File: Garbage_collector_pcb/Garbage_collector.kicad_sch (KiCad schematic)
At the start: 0 parts

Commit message: seance 24 septembre
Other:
- sheet Alim ports: added GPOUT, I2C3_SCL, I2C3_SDA, INT, OTG, STAT, ~{PG}; removed none
- sheet Capteurs et périphériques ports: added I2C1_SCL, I2C1_SDA, Neo_Din, Neo_Dout; removed none
- sheet Moteurs ports: added AIN1, AIN2, BIN1, BIN2, M1_ENCA, M1_ENCB, M2_ENCA, M2_ENCB, Servo1, Servo2, Servo3, ~{FAULT}, ~{SLEEP}; removed none
- sheet STM32 ports: added I2C1_SCL, I2C1_SDA; removed none
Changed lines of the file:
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@@
+			)
+		)
+		(pin "I2C1_SCL" input
+			(at 127 64.77 0)
+			(effects
+				(font
+					(size 1.27 1.27)
+				)
+				(justify right)
+			)
+		)
+		(pin "I2C1_SDA" input
+			(at 127 68.58 0)
+			(effects
+				(font
+					(size 1.27 1.27)
+				)
+				(justify right)
 			)
 		)
@@
 			)
 		)
+		(pin "I2C1_SCL" input
+			(at 195.58 68.58 270)
+			(effects
+				(font
+					(size 1.27 1.27)
+				)
+				(justify left)
+			)
+		)
+		(pin "I2C1_SDA" input
+			(at 198.12 68.58 270)
+			(effects
+				(font
+					(size 1.27 1.27)
+				)
+				(justify left)
+			)
+		)
+		(pin "Neo_Din" input
+			(at 165.1 50.8 180)
+			(effects
+				(font
+					(size 1.27 1.27)
+				)
+				(justify left)
+			)
+		)
+		(pin "Neo_Dout" input
+			(at 165.1 54.61 180)
+			(effects
+				(font
+					(size 1.27 1.27)
+				)
+				(justify left)
+			)
+		)
 		(instances
 			(project "Garbage_collector"
@@
 			)
 		)
+		(pin "GPOUT" output
+			(at 165.1 93.98 180)
+			(effects
+				(font
+					(size 1.27 1.27)
+				)
+				(justify left)
+			)
+		)
+		(pin "I2C3_SCL" input
+			(at 165.1 99.06 180)
+			(effects
+				(font
+					(size 1.27 1.27)
+				)
+				(justify left)
+			)
+		)
+		(pin "I2C3_SDA" input
+			(at 165.1 102.87 180)
+			(effects
+				(font
+					(size 1.27 1.27)
+				)
+				(justify left)
+			)
+		)
+		(pin "INT" output
+			(at 165.1 106.68 180)
+			(effects
+				(font
+					(size 1.27 1.27)
+				)
+				(justify left)
+			)
+		)
+		(pin "OTG" input
+			(at 165.1 110.49 180)
+			(effects
+				(font
+					(size 1.27 1.27)
+				)
+				(justify left)
+			)
+		)
+		(pin "STAT" output
+			(at 165.1 115.57 180)
+			(effects
+				(font
+					(size 1.27 1.27)
+				)
+				(justify left)
+			)
+		)
+		(pin "~{PG}" output
+			(at 165.1 119.38 180)
+			(effects
+				(font
+					(size 1.27 1.27)
+				)
+				(justify left)
+			)
+		)
 		(instances
 			(project "Garbage_collector"
@@
 			)
 		)
+		(pin "AIN1" input
+			(at 128.27 124.46 0)
+			(effects
+				(font
+					(size 1.27 1.27)
+				)
+				(justify right)
+			)
+		)
+		(pin "AIN2" input
+			(at 128.27 127 0)
+			(effects
+				(font
+					(size 1.27 1.27)
+				)
+				(justify right)
+			)
+		)
+		(pin "BIN1" input
+			(at 128.27 129.54 0)
+			(effects
+				(font
+					(size 1.27 1.27)
+				)
+				(justify right)
+			)
+		)
+		(pin "BIN2" input
+			(at 128.27 132.08 0)
+			(effects
+				(font
+					(size 1.27 1.27)
+				)
+				(justify right)
+			)
+		)
+		(pin "M1_ENCA" input
+			(at 128.27 140.97 0)
+			(effects
+				(font
+					(size 1.27 1.27)
+				)
+				(justify right)
+			)
+		)
+		(pin "M1_ENCB" input
+			(at 128.27 143.51 0)
+			(effects
+				(font
+					(size 1.27 1.27)
+				)
+				(justify right)
+			)
+		)
+		(pin "M2_ENCA" input
+			(at 128.27 146.05 0)
+			(effects
+				(font
+					(size 1.27 1.27)
+				)
+				(justify right)
+			)
+		)
+		(pin "M2_ENCB" input
+			(at 128.27 148.59 0)
+			(effects
+				(font
+					(size 1.27 1.27)
+				)
+				(justify right)
+			)
+		)
+		(pin "Servo1" input
+			(at 128.27 113.03 0)
+			(effects
+				(font
+					(size 1.27 1.27)
+				)
+				(justify right)
+			)
+		)
+		(pin "Servo2" input
+			(at 128.27 115.57 0)
+			(effects
+				(font
+					(size 1.27 1.27)
+				)
+				(justify right)
+			)
+		)
+		(pin "Servo3" input
+			(at 128.27 118.11 0)
+			(effects
+				(font
+					(size 1.27 1.27)
+				)
+				(justify right)
+			)
+		)
+		(pin "~{FAULT}" input
+			(at 128.27 157.48 0)
+			(effects
+				(font
+					(size 1.27 1.27)
+				)
+				(justify right)
+			)
+		)
+		(pin "~{SLEEP}" input
+			(at 128.27 154.94 0)
+			(effects
+				(font
+					(size 1.27 1.27)
+				)
+				(justify right)
+			)
+		)

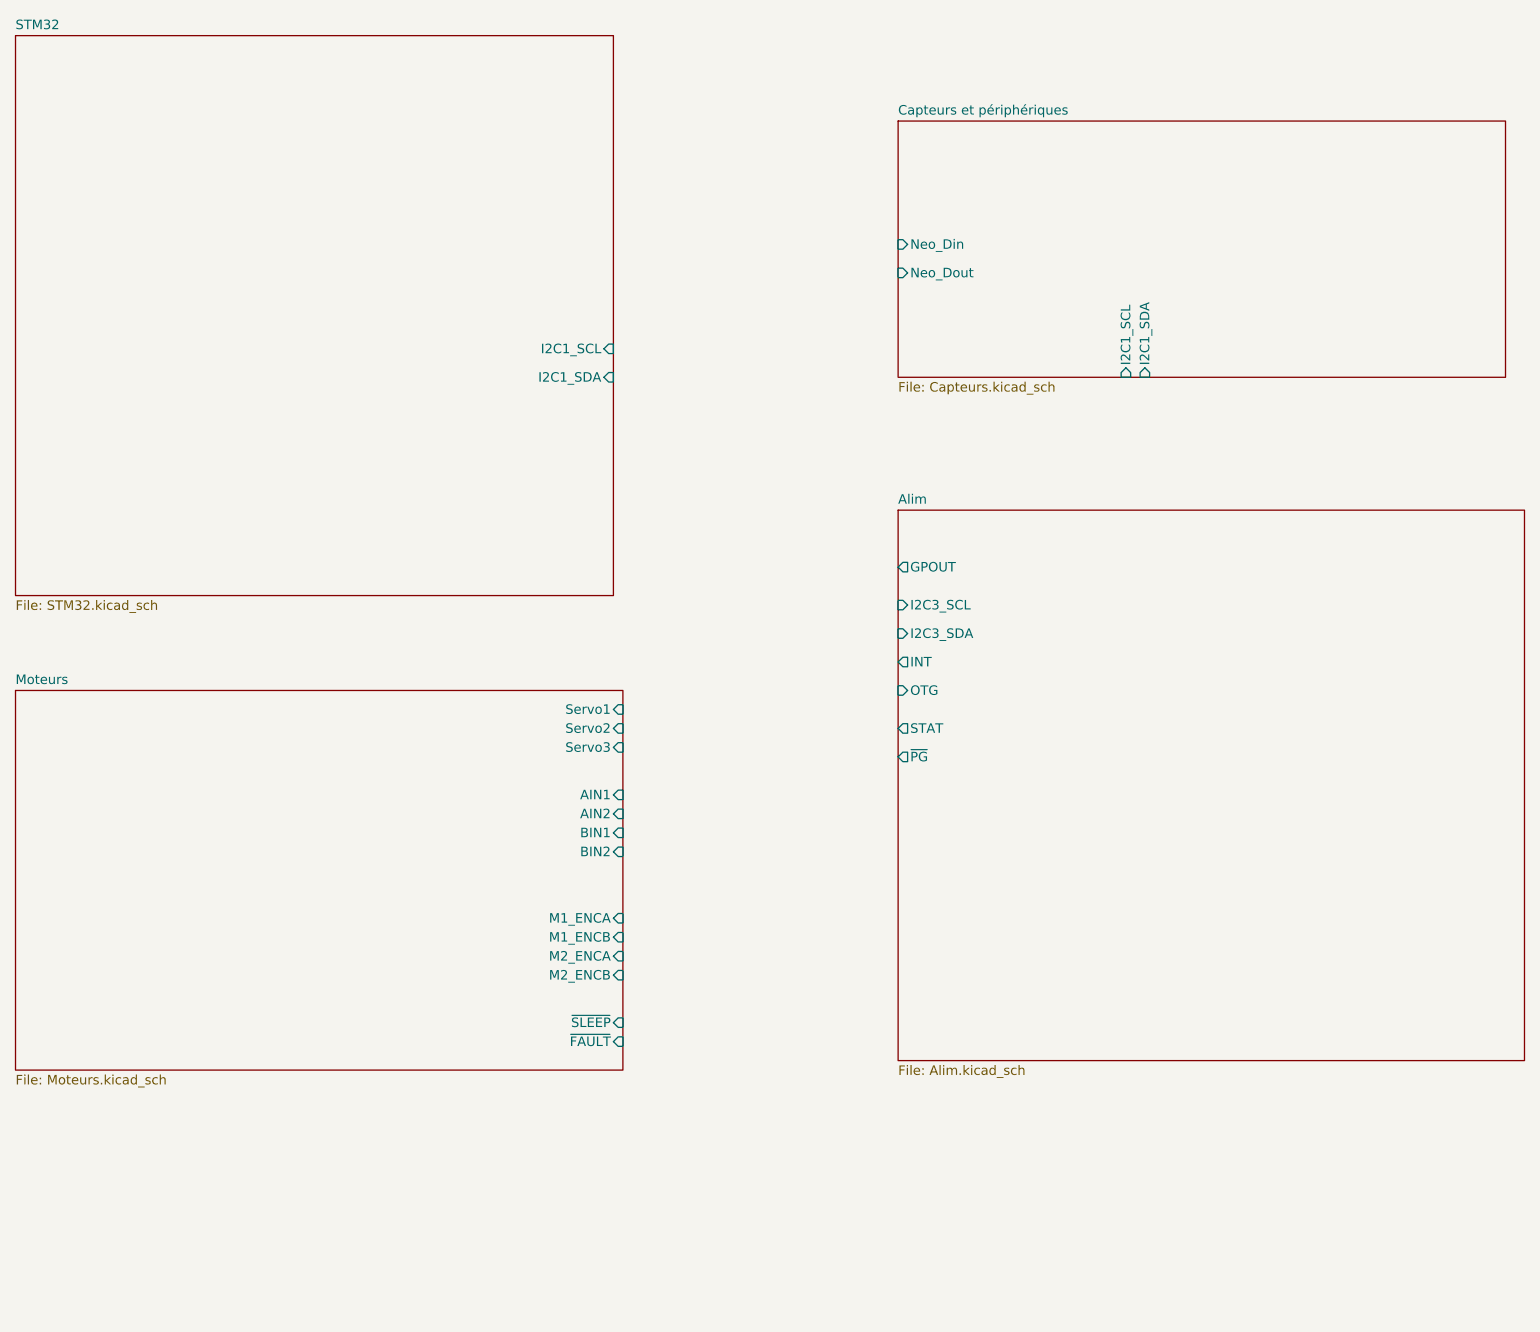
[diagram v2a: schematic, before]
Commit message: update MCU+Moteurs+Capteurs parts + assignement des labels + assignement des pins sur l'ioc (CubeMX)
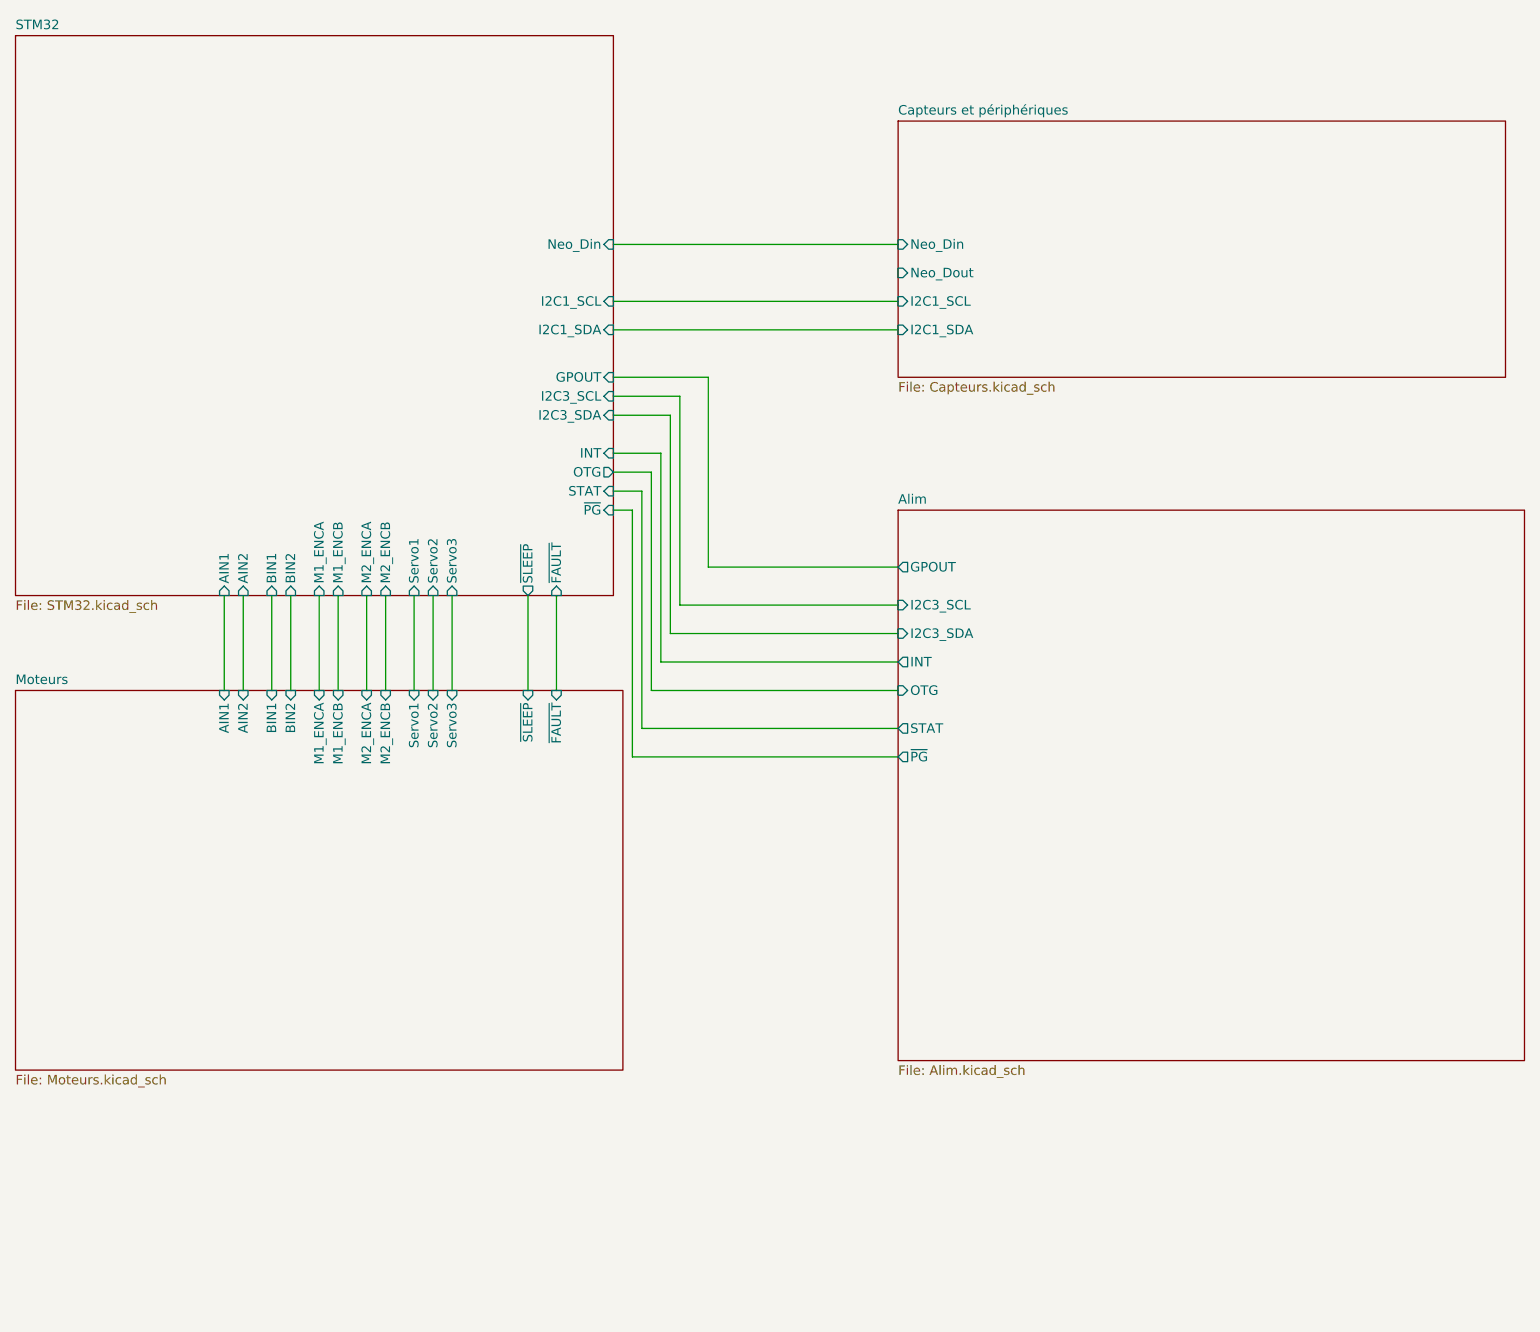
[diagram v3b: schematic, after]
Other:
- sheet STM32 ports: added AIN1, AIN2, BIN1, BIN2, GPOUT, I2C3_SCL, I2C3_SDA, INT, M1_ENCA, M1_ENCB, M2_ENCA, M2_ENCB, Neo_Din, OTG, STAT, Servo1, Servo2, Servo3, ~{FAULT}, ~{PG}, ~{SLEEP}; removed none

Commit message: ajout du ioc et schema validé
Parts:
- added H1, H2, H3, H4: MountingHole_Pad, MountingHole:MountingHole_3.2mm_M3_ISO14580_Pad, symbol Kicad:MountingHole_Pad
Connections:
- new net GND: H1.1, H2.1, H3.1, H4.1
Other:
- sheet Alim ports: added CHARGEUR_INT, CHARGEUR_PG, CHARGEUR_QON, FG_GPIO; removed GPOUT, INT, OTG, STAT, ~{PG}
- sheet Capteurs et périphériques ports: added COLOR_INT, Lidar_M_CTRL, Lidar_TX, TOF1_INT, TOF1_XST, TOF2_INT, TOF2_XST; removed Neo_Dout
- sheet Moteurs ports: added MOTOR_FAULT, MOTOR_SLEEP; removed Servo3, ~{FAULT}, ~{SLEEP}
- sheet STM32 ports: added CHARGEUR_INT, CHARGEUR_PG, COLOR_INT, FG_GPIO, Lidar_M_CTRL, Lidar_TX, MOTOR_FAULT, MOTOR_SLEEP, TOF1_INT, TOF1_XST, TOF2_INT, TOF2_XST; removed GPOUT, INT, OTG, STAT, Servo3, ~{FAULT}, ~{PG}, ~{SLEEP}

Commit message: finalisation des empreintes
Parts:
- renumbered H3 to H1, H1 to H3
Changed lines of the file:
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@@
 		(dnp no)
 		(fields_autoplaced yes)
-		(property "Reference" "H3"
+		(property "Reference" "H1"
 			(at 57.15 180.3399 0)
 			(show_name no)
@@
 			(project "Garbage_collector"
 				(path "/158d6e2c-2f49-4796-8b5c-460e7c4b776f"
-					(reference "H3")
+					(reference "H1")
 					(unit 1)
 				)
@@
 		(dnp no)
 		(fields_autoplaced yes)
-		(property "Reference" "#PWR068"
+		(property "Reference" "#PWR01"
 			(at 67.31 194.31 0)
 			(hide yes)
@@
 			(project "Garbage_collector"
 				(path "/158d6e2c-2f49-4796-8b5c-460e7c4b776f"
-					(reference "#PWR068")
+					(reference "#PWR01")
 					(unit 1)
 				)
@@
 		(dnp no)
 		(fields_autoplaced yes)
-		(property "Reference" "H1"
+		(property "Reference" "H3"
 			(at 80.01 180.3399 0)
 			(show_name no)
@@
 			(project "Garbage_collector"
 				(path "/158d6e2c-2f49-4796-8b5c-460e7c4b776f"
-					(reference "H1")
+					(reference "H3")
 					(unit 1)
 				)

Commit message: fin du routage
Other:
- sheet Alim ports: added Chargeur_OTG; removed CHARGEUR_PG
- sheet STM32 ports: added CHARGEUR_QON, Chargeur_OTG; removed CHARGEUR_PG
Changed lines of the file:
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@@
+	(wire
+		(pts
+			(xy 127 86.36) (xy 165.1 86.36)
+		)
+		(stroke
+			(width 0)
+			(type default)
+		)
+	)
 	(wire
 		(pts
@@
 			)
 		)
+		(pin "MOTOR_FAULT" input
+			(at 66.04 97.79 270)
+			(effects
+				(font
+					(size 1.27 1.27)
+				)
+				(justify left)
+			)
+		)
+		(pin "COLOR_INT" input
+			(at 127 27.94 0)
+			(effects
+				(font
+					(size 1.27 1.27)
+				)
+				(justify right)
+			)
+		)
+		(pin "Lidar_M_CTRL" input
+			(at 127 33.02 0)
+			(effects
+				(font
+					(size 1.27 1.27)
+				)
+				(justify right)
+			)
+		)
+		(pin "Lidar_TX" input
+			(at 127 35.56 0)
+			(effects
+				(font
+					(size 1.27 1.27)
+				)
+				(justify right)
+			)
+		)
+		(pin "TOF1_INT" input
+			(at 127 41.91 0)
+			(effects
+				(font
+					(size 1.27 1.27)
+				)
+				(justify right)
+			)
+		)
+		(pin "TOF1_XST" input
+			(at 127 44.45 0)
+			(effects
+				(font
+					(size 1.27 1.27)
+				)
+				(justify right)
+			)
+		)
+		(pin "TOF2_INT" input
+			(at 127 46.99 0)
+			(effects
+				(font
+					(size 1.27 1.27)
+				)
+				(justify right)
+			)
+		)
+		(pin "TOF2_XST" input
+			(at 127 49.53 0)
+			(effects
+				(font
+					(size 1.27 1.27)
+				)
+				(justify right)
+			)
+		)
 		(pin "CHARGEUR_INT" input
 			(at 127 92.71 0)
@@
 			)
 		)
-		(pin "CHARGEUR_PG" input
+		(pin "Chargeur_OTG" input
 			(at 127 95.25 0)
 			(effects
@@
 			)
 		)
-		(pin "MOTOR_FAULT" input
-			(at 66.04 97.79 270)
-			(effects
-				(font
-					(size 1.27 1.27)
-				)
-				(justify left)
-			)
-		)
-		(pin "COLOR_INT" input
-			(at 127 27.94 0)
-			(effects
-				(font
-					(size 1.27 1.27)
-				)
-				(justify right)
-			)
-		)
-		(pin "Lidar_M_CTRL" input
-			(at 127 33.02 0)
-			(effects
-				(font
-					(size 1.27 1.27)
-				)
-				(justify right)
-			)
-		)
-		(pin "Lidar_TX" input
-			(at 127 35.56 0)
-			(effects
-				(font
-					(size 1.27 1.27)
-				)
-				(justify right)
-			)
-		)
-		(pin "TOF1_INT" input
-			(at 127 41.91 0)
-			(effects
-				(font
-					(size 1.27 1.27)
-				)
-				(justify right)
-			)
-		)
-		(pin "TOF1_XST" input
-			(at 127 44.45 0)
-			(effects
-				(font
-					(size 1.27 1.27)
-				)
-				(justify right)
-			)
-		)
-		(pin "TOF2_INT" input
-			(at 127 46.99 0)
-			(effects
-				(font
-					(size 1.27 1.27)
-				)
-				(justify right)
-			)
-		)
-		(pin "TOF2_XST" input
-			(at 127 49.53 0)
+		(pin "CHARGEUR_QON" input
+			(at 127 86.36 0)
 			(effects
 				(font
@@
 			)
 		)
-		(pin "CHARGEUR_PG" output
+		(pin "CHARGEUR_QON" input
+			(at 165.1 86.36 180)
+			(effects
+				(font
+					(size 1.27 1.27)
+				)
+				(justify left)
+			)
+		)
+		(pin "Chargeur_OTG" input
 			(at 165.1 95.25 180)
 			(effects
 				(font
-					(size 1.27 1.27)
-				)
-				(justify left)
-			)
-		)
-		(pin "CHARGEUR_QON" input
-			(at 165.1 105.41 180)
-			(effects
-				(font
